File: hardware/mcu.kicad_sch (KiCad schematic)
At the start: 17 parts

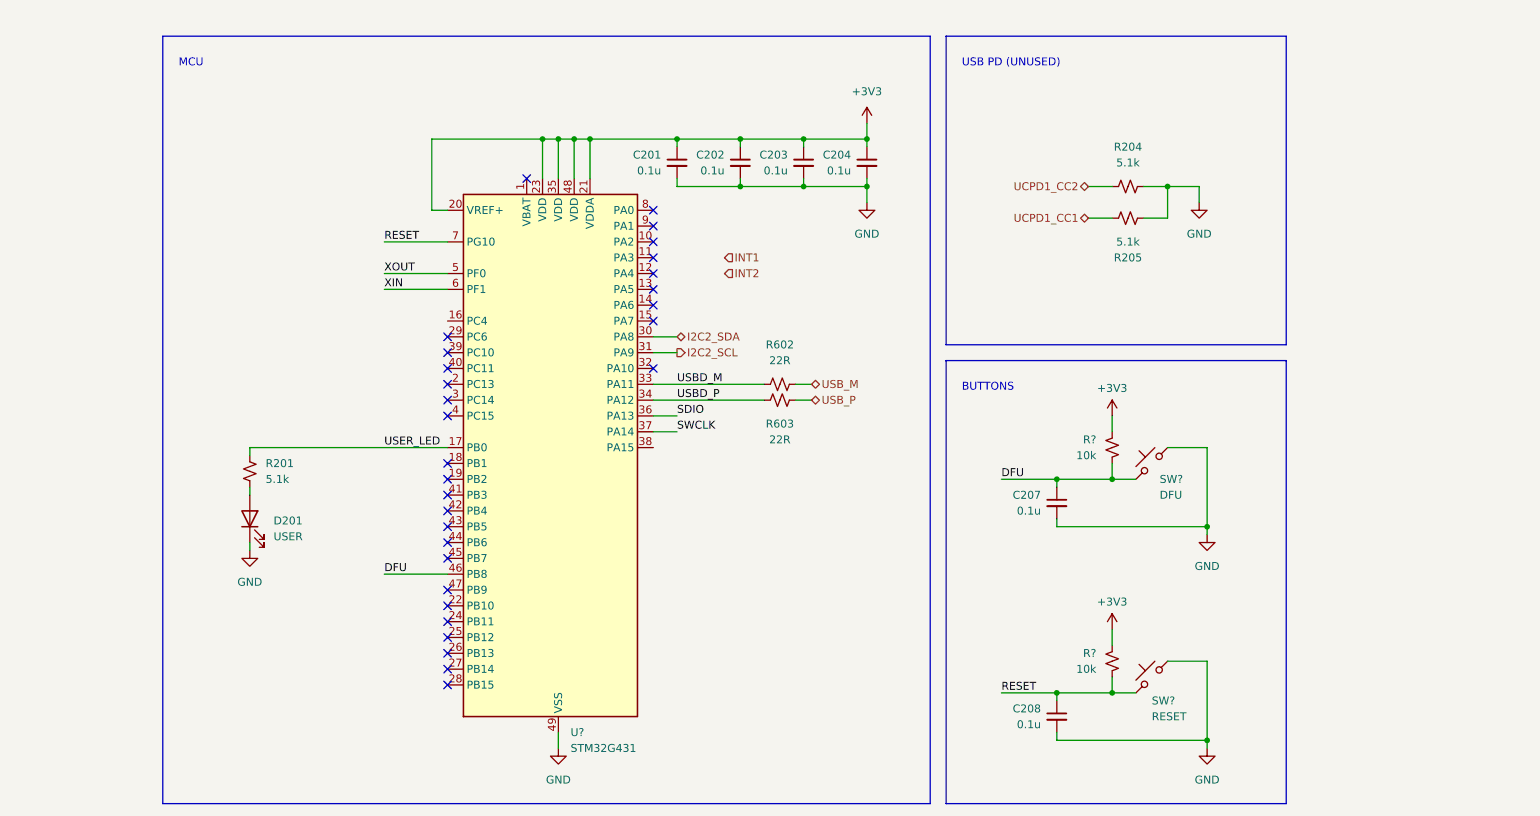
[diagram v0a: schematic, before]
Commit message: new hardware layout for IIS2ICLX
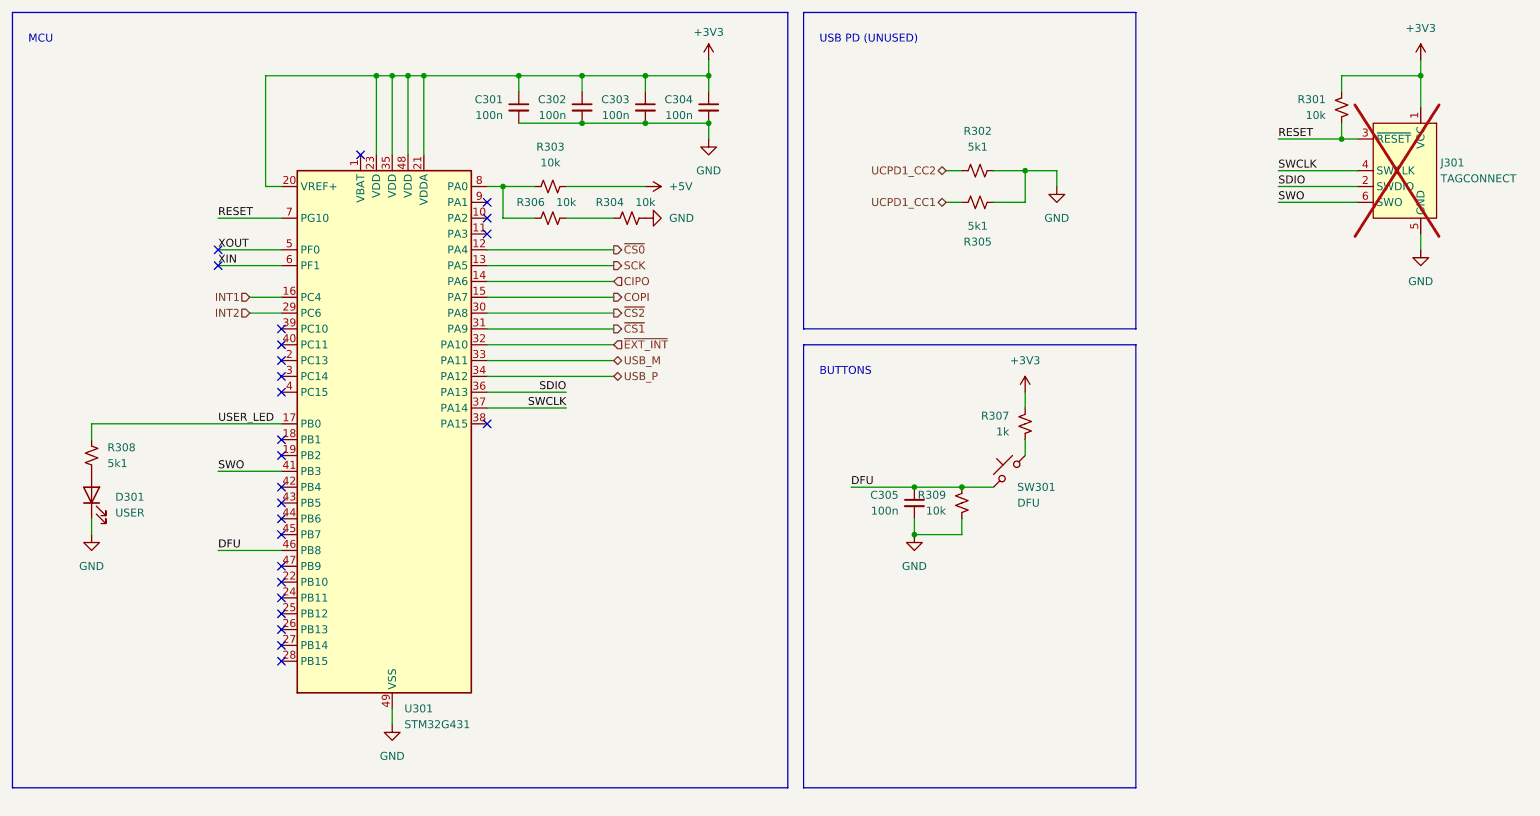
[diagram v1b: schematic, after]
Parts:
- removed C208: 0.1u, Capacitor_SMD:C_0402_1005Metric, symbol Device:C_Small
- removed R602, R603: 22R, Resistor_SMD:R_0402_1005Metric, symbol Device:R_Small_US
- removed SW?: RESET, matei:TS-1187A-B-A-B, symbol Switch:SW_Push_45deg
- added J301: TAGCONNECT, Connector:Tag-Connect_TC2030-IDC-NL_2x03_P1.27mm_Vertical, symbol Connector:Conn_ARM_SWD_TagConnect_TC2030-NL
- added R303, R304, R306, R309: 10k, Resistor_SMD:R_0402_1005Metric, symbol Device:R_Small_US
- C301: renamed from C201; value 0.1u -> 100n; LCSC ID (none) -> C1525
- C302: renamed from C202; value 0.1u -> 100n; LCSC ID (none) -> C1525
- C303: renamed from C203; value 0.1u -> 100n; LCSC ID (none) -> C1525
- C304: renamed from C204; value 0.1u -> 100n; LCSC ID (none) -> C1525
- C305: renamed from C207; value 0.1u -> 100n; LCSC ID (none) -> C1525
- D301: renamed from D201; LCSC ID (none) -> C2290
- R301: renamed from R?; LCSC ID (none) -> C25744
- R302: renamed from R204; value 5.1k -> 5k1; LCSC ID (none) -> C25905
- R305: renamed from R205; value 5.1k -> 5k1; LCSC ID (none) -> C25905
- R307: renamed from R?; value 10k -> 1k; LCSC ID (none) -> C11702
- R308: renamed from R201; value 5.1k -> 5k1; LCSC ID (none) -> C25905
- SW301: renamed from SW?; LCSC ID (none) -> C318884
- U301: renamed from U?; LCSC ID (none) -> C529356
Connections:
- net USBD_M is gone; now on net USB_M: U301.33 (PA11)
- net USBD_P is gone; now on net USB_P: U301.34 (PA12)
- net +3V3: now also J301.1 (VCC)
- net DFU: now also R309.1; no longer R307.2
- net GND: now also J301.5 (GND), R304.2, R309.2; no longer SW301.2
- net INT1: now also U301.16 (PC4)
- net INT2: now also U301.29 (PC6)
- net RESET: now also J301.3 (~{RESET})
- net SDIO: now also J301.2 (SWDIO)
- net SWCLK: now also J301.4 (SWCLK)
- net ~{CS0}: now reaches U301.12 (PA4)
- net SCK: now reaches U301.13 (PA5)
- net CIPO: now reaches U301.14 (PA6)
- net COPI: now reaches U301.15 (PA7)
- net ~{EXT_INT}: now reaches U301.32 (PA10)
- net SWO: now reaches U301.41 (PB3)
- net SWO: now also J301.6 (SWO)
- net at U301.8 (PA0): now also R303.1, R306.1
- net I2C2_SCL renamed ~{CS1}
- net I2C2_SDA renamed ~{CS2}
- new net: R307.2, SW301.2
- new net: R304.1, R306.2
- new net +5V: R303.2
- no-connect marks 30 -> 25
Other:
- moved on the sheet: C301, C302, C303, C304, C305, D301, R301, R302, R305, R307, R308, SW301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
